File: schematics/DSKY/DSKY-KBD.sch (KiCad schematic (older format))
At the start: 63 parts, among them SW1 SW_Push, SW10 SW_Push, SW11 SW_Push, SW12 SW_Push, SW13 SW_Push, SW14 SW_Push, SW15 SW_Push, SW16 SW_Push, SW17 SW_Push, SW18 SW_Push, SW19 SW_Push, SW2 SW_Push, SW3 SW_Push, SW4 SW_Push, SW5 SW_Push, SW6 SW_Push, SW7 SW_Push, SW8 SW_Push, SW9 SW_Push, U1 74LS273, U10 74LS20, U11 74LS20, U12 74LS20, U13 74LS02, U14 74LS27, U15 74LS27, U16 74LS74, U17 74LS32, U18 74LS126, U2 74LS244, U3 LM555, U4 74LS04, U40 74LS32, U5 74LS04, U6 74LS00, U7 74LS00, U8 74LS10, U9 74LS20

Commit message: Add files via upload
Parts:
- R2: value 4k -> 3.9K
- R3: value 8k -> 8.2K
- renumbered U18 to U47
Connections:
- net CH14: now also U47.6; no longer U47.3
- net at U40.6: now also U47.4; no longer U47.1
- net at U16.9 (Q): now also U47.5; no longer U47.2
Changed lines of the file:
@@
 AR Path="/60F98A72/66CE2F9E/678084E5" Ref="R?"  Part="1"
 F 0 "R2" H 6218 6696 50  0000 L CNN
-F 1 "4k" H 6218 6605 50  0000 L CNN
+F 1 "3.9K" H 6218 6605 50  0000 L CNN
 F 2 "" V 6190 6640 50  0001 C CNN
 F 3 "~" H 6150 6650 50  0001 C CNN
@@
 AR Path="/60F98A72/66CE2F9E/678084EE" Ref="R?"  Part="1"
 F 0 "R3" H 6000 7150 50  0000 L CNN
-F 1 "8k" H 6000 7050 50  0000 L CNN
+F 1 "8.2K" H 6000 7050 50  0000 L CNN
 F 2 "" V 6190 7090 50  0001 C CNN
 F 3 "~" H 6150 7100 50  0001 C CNN
@@
 	8800 4600 9600 4600
 $Comp
-L 74xx:74LS126 U18
-U 1 1 62A3E22F
+L 74xx:74LS126 U47
+U 2 1 62A3E22F
 P 9250 6100
-F 0 "U18" H 9250 6417 50  0000 C CNN
+F 0 "U47" H 9250 6417 50  0000 C CNN
 F 1 "74LS126" H 9250 6326 50  0000 C CNN
 F 2 "" H 9250 6100 50  0001 C CNN
 F 3 "http://www.ti.com/lit/gpn/sn74LS126" H 9250 6100 50  0001 C CNN
-	1    9250 6100
-	1    0    0    -1
-$EndComp
+	2    9250 6100
+	1    0    0    -1
+$EndComp

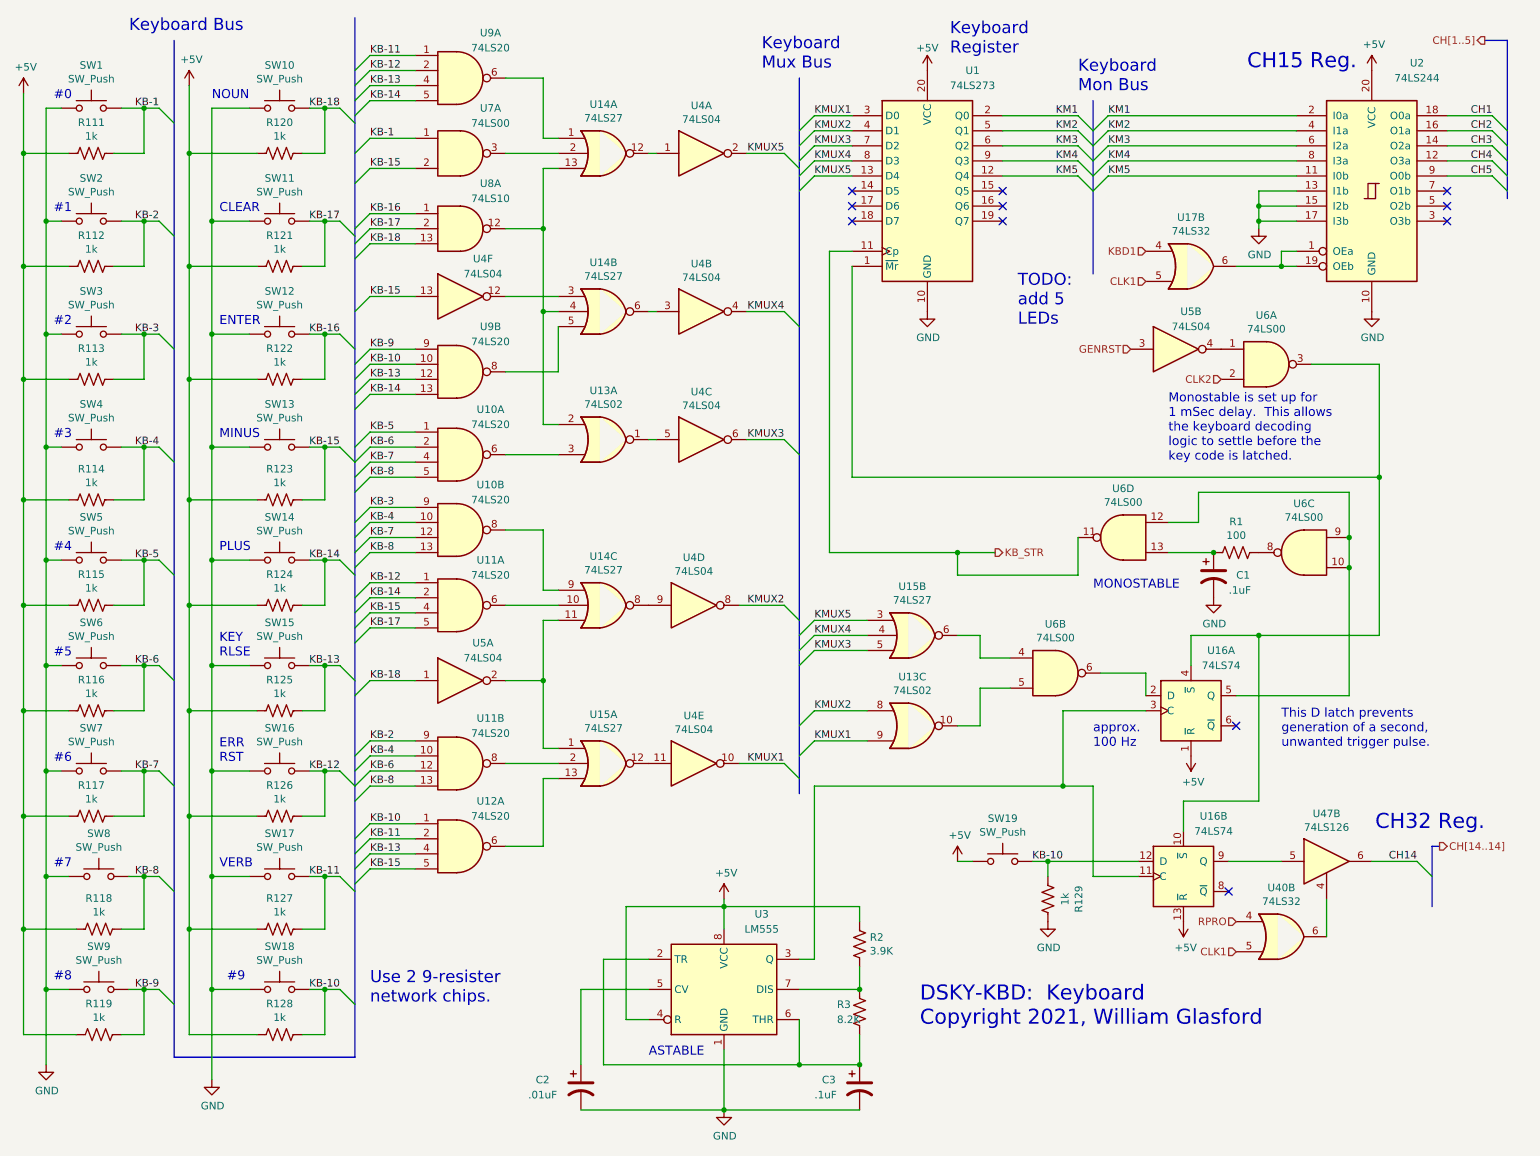
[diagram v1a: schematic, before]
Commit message: Minor tweaks to the display decoding logic.
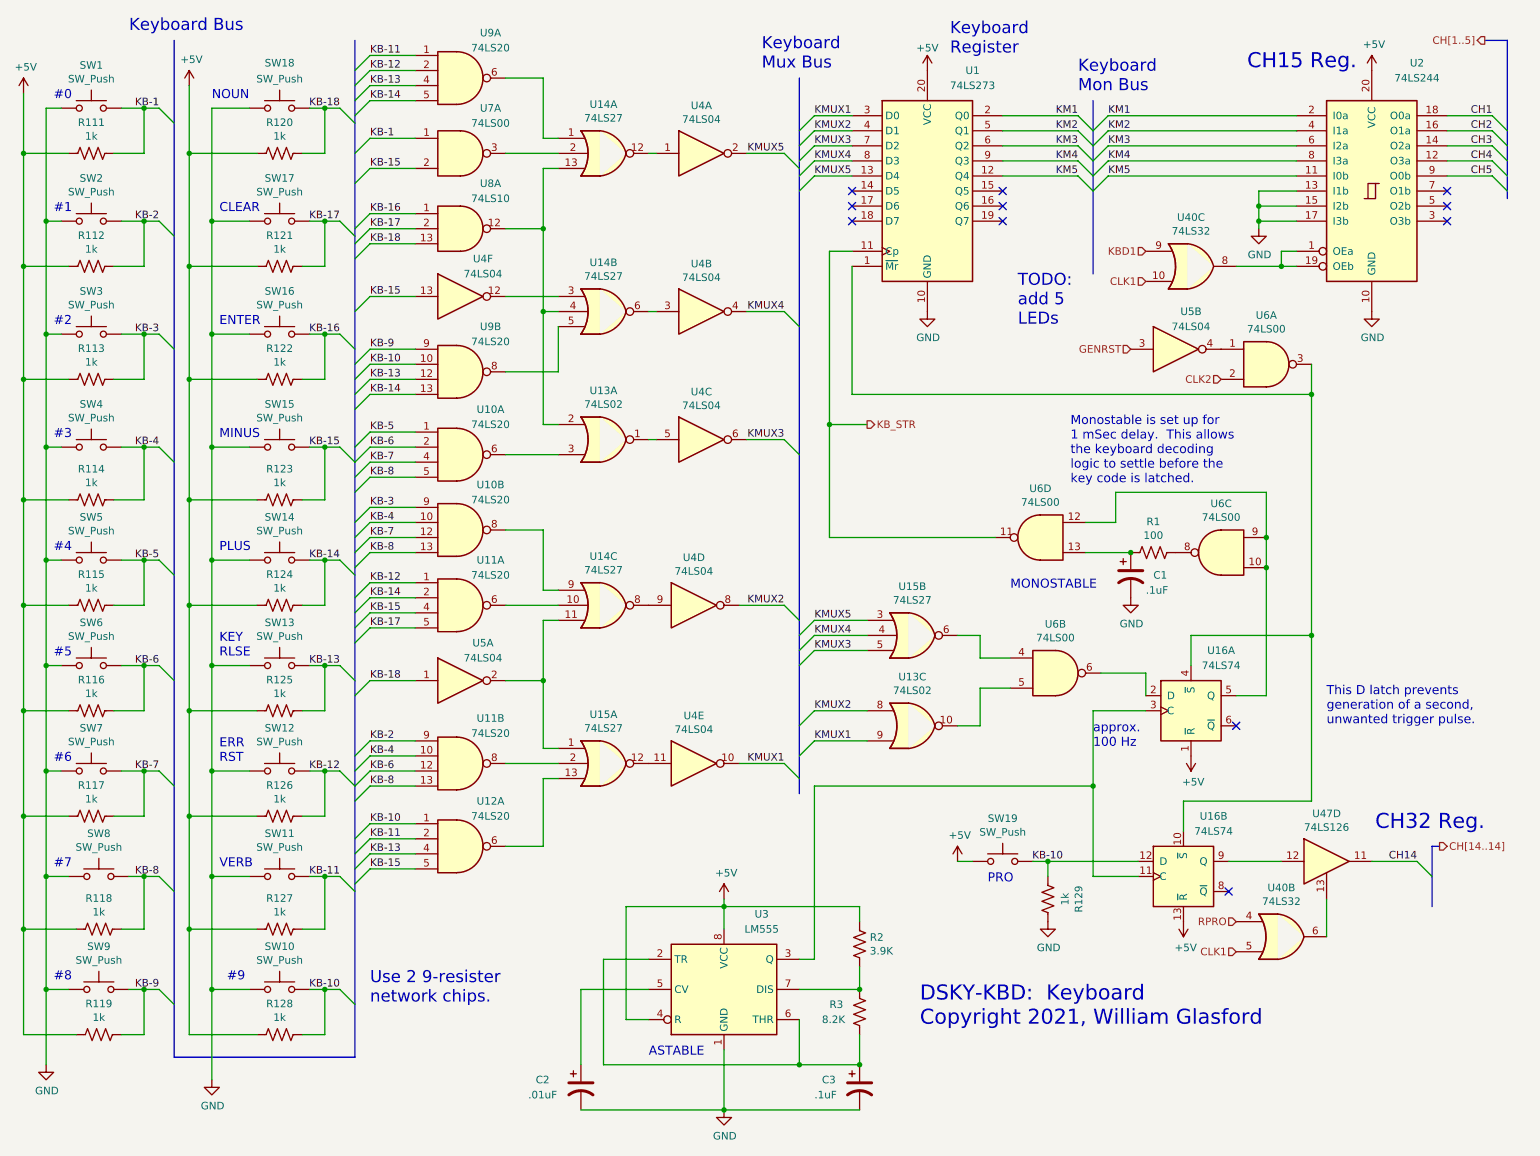
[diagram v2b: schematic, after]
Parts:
- renumbered SW18 to SW10, SW17 to SW11, SW16 to SW12, SW15 to SW13, SW13 to SW15, SW12 to SW16, SW11 to SW17, SW10 to SW18, U17 to U40
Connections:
- net CH14: now also U47.11; no longer U47.6
- net CLK1: now also U40.10; no longer U40.5
- net KBD1: now also U40.9; no longer U40.4
- net at U40.6: now also U47.13; no longer U47.4
- net at U16.9 (Q): now also U47.12; no longer U47.5
- net at U2.1 (OEa), U2.19 (OEb): now also U40.8; no longer U40.6
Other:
- note added: "PRO"
- moved on the sheet: C1, R1, U6C, U6D

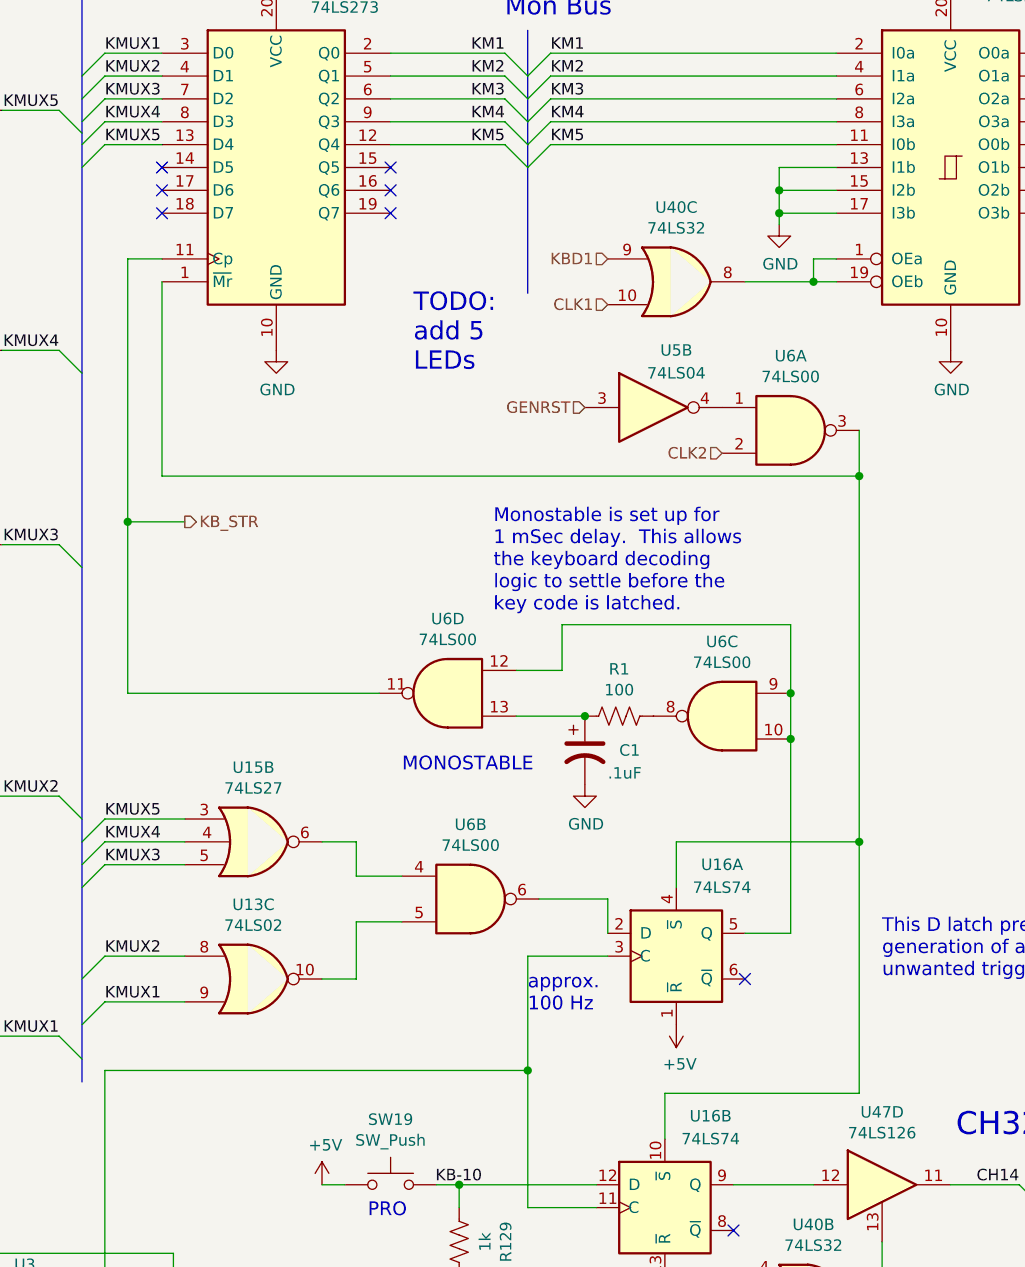
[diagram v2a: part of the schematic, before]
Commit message: Simplified reset lines.
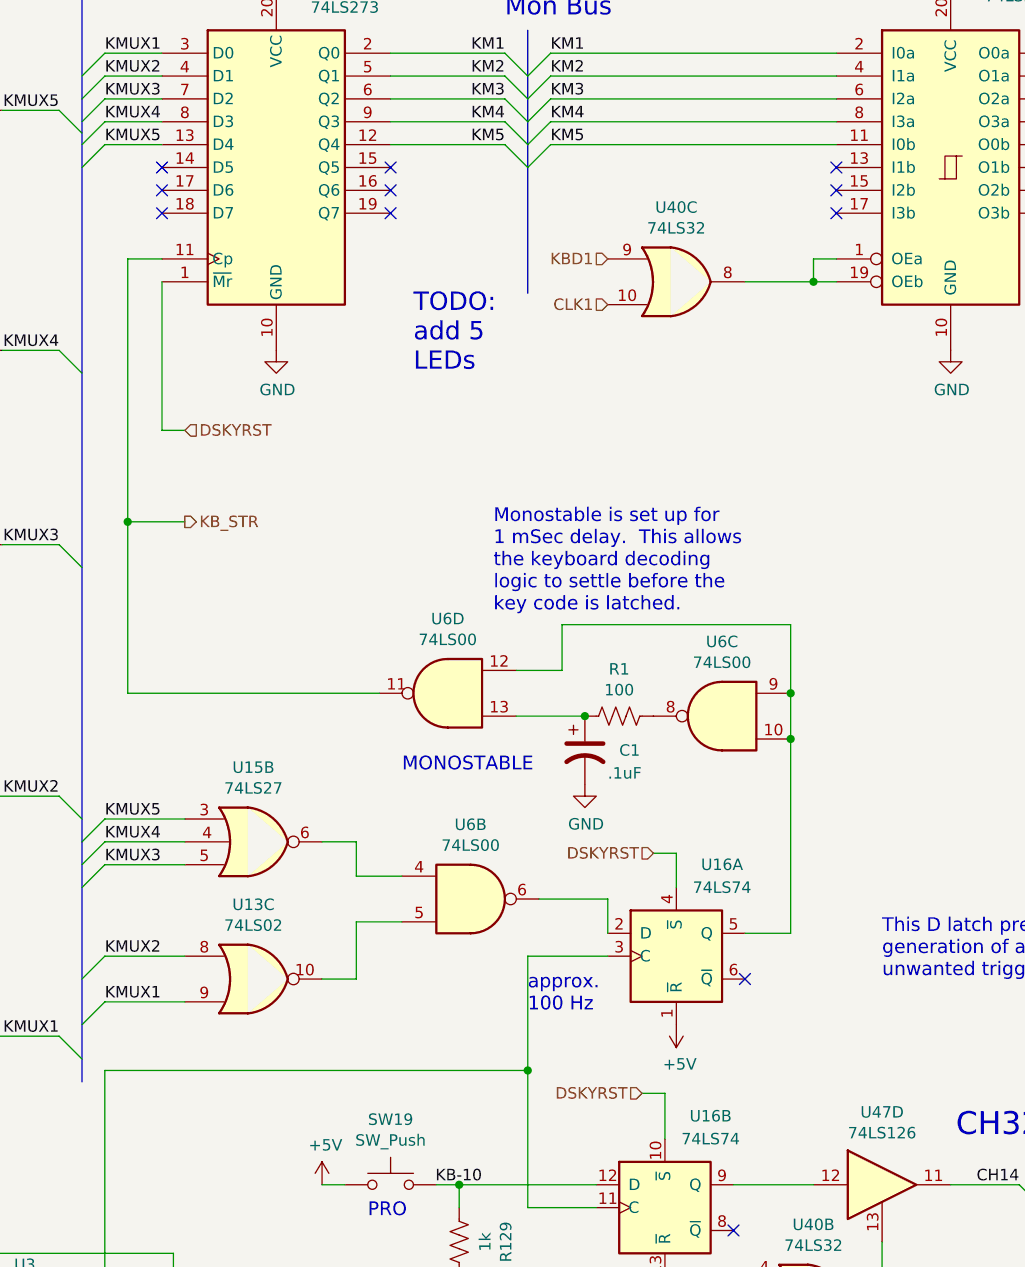
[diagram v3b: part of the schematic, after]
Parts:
- removed unit 2 of U5
- removed unit 1 of U6
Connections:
- net GND: no longer U2.13 (I1b), U2.15 (I2b), U2.17 (I3b)
- net DSKYRST: now reaches U1.1 (~Mr), U16.10 (~S), U16.4 (~S)
- no-connect marks 11 -> 14
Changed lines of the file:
@@
 KMUX5
 Wire Wire Line
-	6100 2150 6100 3000
+	6100 2150 6100 2800
 Wire Wire Line
 	6100 2050 5950 2050
@@
 Wire Wire Line
 	8650 5000 8850 5000
-Text HLabel 7950 2700 0    50   Input ~ 0
-GENRST
-Wire Wire Line
-	8350 4600 8350 4800
+Text HLabel 8200 5700 0    50   Input ~ 0
+DSKYRST
 Wire Wire Line
 	5850 5600 5850 6750
@@
 Wire Wire Line
 	7850 3850 7650 3850
-Text HLabel 8550 2900 0    50   Input ~ 0
-CLK2
-$Comp
-L 74xx:74LS00 U?
-U 1 1 6780854A
-P 8850 2800
-AR Path="/5F5E4E3B/5F5F8347/6780854A" Ref="U?"  Part="1"
-AR Path="/60F98A72/6780854A" Ref="U6"  Part="1"
-AR Path="/66BEE9C8/6780854A" Ref="U?"  Part="1"
-AR Path="/60F98A72/66CE2F9E/6780854A" Ref="U?"  Part="1"
-F 0 "U6" H 8850 3125 50  0000 C CNN
-F 1 "74LS00" H 8850 3034 50  0000 C CNN
-F 2 "" H 8850 2800 50  0001 C CNN
-F 3 "http://www.ti.com/lit/gpn/sn74ls00" H 8850 2800 50  0001 C CNN
-	1    8850 2800
-	1    0    0    -1
-$EndComp
-$Comp
-L 74xx:74LS04 U?
-U 2 1 67808550
-P 8250 2700
-AR Path="/5F5E4E3B/5F5F8347/67808550" Ref="U?"  Part="6"
-AR Path="/60F98A72/67808550" Ref="U5"  Part="2"
-AR Path="/66BEE9C8/67808550" Ref="U?"  Part="6"
-AR Path="/60F98A72/66CE2F9E/67808550" Ref="U?"  Part="6"
-F 0 "U5" H 8350 2950 50  0000 C CNN
-F 1 "74LS04" H 8350 2850 50  0000 C CNN
-F 2 "" H 8250 2700 50  0001 C CNN
-F 3 "http://www.ti.com/lit/gpn/sn74LS04" H 8250 2700 50  0001 C CNN
-	2    8250 2700
-	1    0    0    -1
-$EndComp
 Text Notes 1300 600  0    80   ~ 0
 Keyboard Bus
@@
 	7700 5100 7700 5600
 Wire Wire Line
-	6100 3000 9150 3000
-Wire Wire Line
-	9150 2800 9150 3000
+	6100 2800 6200 2800
 $Comp
 L 74xx:74LS244 U?
@@
 $EndComp
 Wire Wire Line
-	8800 1900 8800 1850
-$Comp
-L power:GND #PWR?
-U 1 1 678085AB
-P 8800 1900
-AR Path="/60F98A1A/678085AB" Ref="#PWR?"  Part="1"
-AR Path="/66BEEA04/678085AB" Ref="#PWR?"  Part="1"
-AR Path="/60F98A72/66CE2FA0/678085AB" Ref="#PWR?"  Part="1"
-AR Path="/60F98A72/66CE2F9E/678085AB" Ref="#PWR?"  Part="1"
-AR Path="/60F98A72/678085AB" Ref="#PWR0257"  Part="1"
-F 0 "#PWR0257" H 8800 1650 50  0001 C CNN
-F 1 "GND" H 8805 1727 50  0000 C CNN
-F 2 "" H 8800 1900 50  0001 C CNN
-F 3 "" H 8800 1900 50  0001 C CNN
-	1    8800 1900
-	1    0    0    -1
-$EndComp
-Wire Wire Line
 	8650 2150 8950 2150
-Wire Wire Line
-	8800 1650 9050 1650
-Wire Wire Line
-	8800 1750 9050 1750
-Wire Wire Line
-	8800 1850 9050 1850
 Wire Wire Line
 	8950 2150 9050 2150
@@
 NoConn ~ 10050 1750
 NoConn ~ 10050 1850
-Connection ~ 8800 1750
-Wire Wire Line
-	8800 1750 8800 1650
-Connection ~ 8800 1850
-Wire Wire Line
-	8800 1850 8800 1750
 Wire Wire Line
 	7100 1550 7600 1550
@@
 Use 2 9-resister\nnetwork chips.
 Wire Wire Line
-	8300 5700 9150 5700
-Wire Wire Line
-	9150 5700 9150 4600
+	8300 5700 8200 5700
 $Comp
 L 74xx:74LS126 U47
@@
 	9250 6350 9250 6600
 Wire Wire Line
-	9150 3000 9150 4600
-Wire Wire Line
 	5950 3950 7050 3950
 Connection ~ 5950 3200
@@
 Wire Wire Line
 	8850 4150 8850 5000
-Connection ~ 9150 3000
-Connection ~ 9150 4600
-Wire Wire Line
-	8350 4600 9150 4600
+Wire Wire Line
+	8350 4650 8250 4650
 Connection ~ 7700 5600
 Wire Wire Line
@@
 Text Notes 7000 6250 0    60   ~ 0
 PRO
+NoConn ~ 9050 1650
+NoConn ~ 9050 1750
+NoConn ~ 9050 1850
+Text HLabel 8250 4650 0    50   Input ~ 0
+DSKYRST
+Text HLabel 6200 2800 2    50   Input ~ 0
+DSKYRST
+Wire Wire Line
+	8350 4650 8350 4800
 Wire Bus Line
 	9950 6000 9950 6400

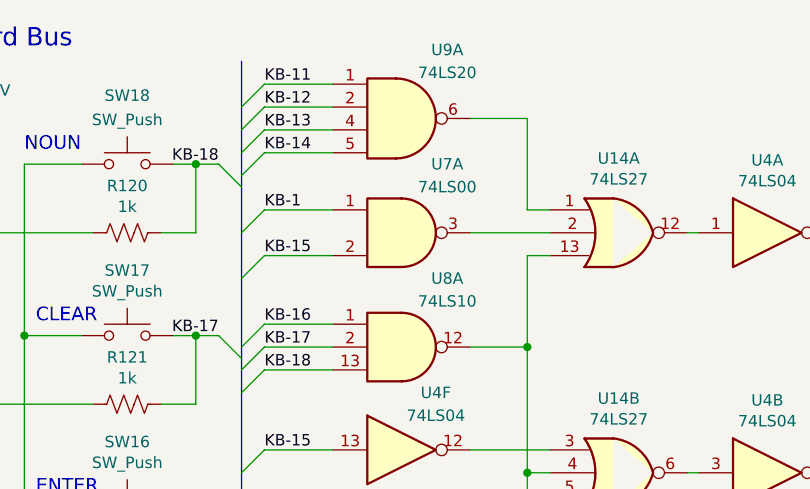
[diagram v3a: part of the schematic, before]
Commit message: Cleaned up clock logic.
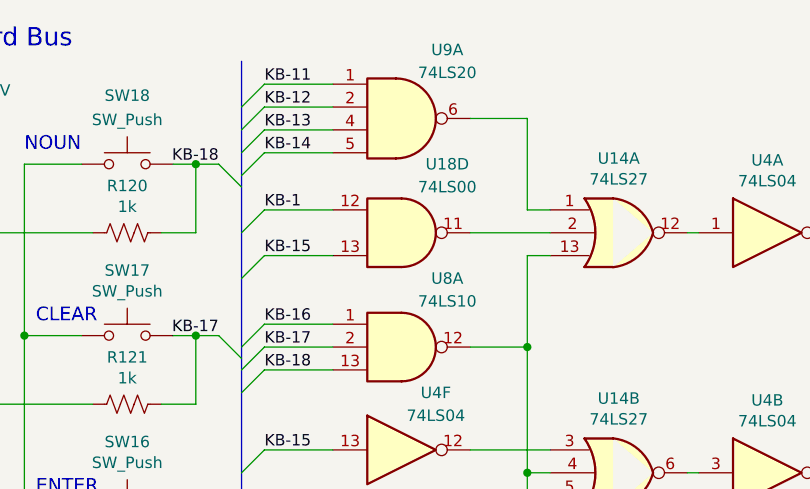
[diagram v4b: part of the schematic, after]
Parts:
- removed U7: 74LS00, symbol 74xx:74LS00
- added U18: 74LS00, symbol 74xx:74LS00
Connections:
- net KB-1: now also U18.12
- net KB-15: now also U18.13
- net at U14.2: now also U18.11
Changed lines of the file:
@@
 Wire Wire Line
 	3200 1500 2900 1500
-$Comp
-L 74xx:74LS00 U7
-U 1 1 64CA909C
-P 3500 1400
-F 0 "U7" H 3700 1700 50  0000 C CNN
-F 1 "74LS00" H 3700 1600 50  0000 C CNN
-F 2 "" H 3500 1400 50  0001 C CNN
-F 3 "http://www.ti.com/lit/gpn/sn74ls00" H 3500 1400 50  0001 C CNN
-	1    3500 1400
-	1    0    0    -1
-$EndComp
 Connection ~ 4050 1900
 Wire Wire Line
@@
 Wire Bus Line
 	2800 650  2800 7400
+$Comp
+L 74xx:74LS00 U18
+U 4 1 614FF2D5
+P 3500 1400
+F 0 "U18" H 3700 1700 50  0000 C CNN
+F 1 "74LS00" H 3700 1600 50  0000 C CNN
+F 2 "" H 3500 1400 50  0001 C CNN
+F 3 "http://www.ti.com/lit/gpn/sn74ls00" H 3500 1400 50  0001 C CNN
+	4    3500 1400
+	1    0    0    -1
+$EndComp
 $EndSCHEMATC
